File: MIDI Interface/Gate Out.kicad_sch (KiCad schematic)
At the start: 11 parts, among them J3 AudioJack2_SwitchT, U2 TL074

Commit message: Start MIDI interface board
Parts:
- C301: renamed from C25; footprint (none) -> 0_Capacitor_THT:C_Disc_D5.5mm_W2.5mm_P2.50mm
- C302: renamed from C26; footprint (none) -> 0_Capacitor_THT:C_Disc_D5.5mm_W2.5mm_P2.50mm
- D301: renamed from D8; footprint (none) -> LED_THT:LED_D5.0mm
- J301: renamed from J3; symbol Connector:AudioJack2_SwitchT -> Connector_Audio:AudioJack2_SwitchT
- R301: renamed from R7; footprint (none) -> Resistor_THT:R_Axial_DIN0207_L6.3mm_D2.5mm_P7.62mm_Horizontal
- R302: renamed from R8; footprint (none) -> Resistor_THT:R_Axial_DIN0207_L6.3mm_D2.5mm_P7.62mm_Horizontal
- R303: renamed from R9; footprint (none) -> Resistor_THT:R_Axial_DIN0207_L6.3mm_D2.5mm_P7.62mm_Horizontal
- R304: renamed from R10; footprint (none) -> Resistor_THT:R_Axial_DIN0207_L6.3mm_D2.5mm_P7.62mm_Horizontal
- R305: renamed from R11; footprint (none) -> Resistor_THT:R_Axial_DIN0207_L6.3mm_D2.5mm_P7.62mm_Horizontal
- R306: renamed from R12; footprint (none) -> Resistor_THT:R_Axial_DIN0207_L6.3mm_D2.5mm_P7.62mm_Horizontal
- U202: renamed from U2; footprint (none) -> Package_DIP:DIP-14_W7.62mm_Socket

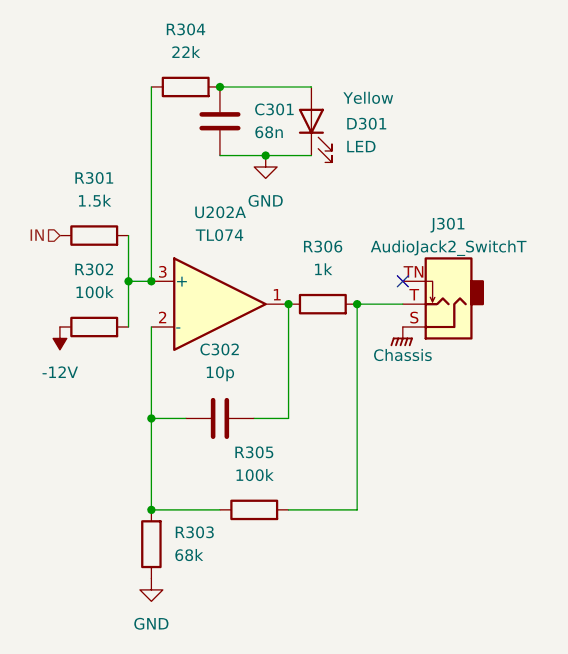
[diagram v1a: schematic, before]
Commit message: New MIDI controller, new envelope generator
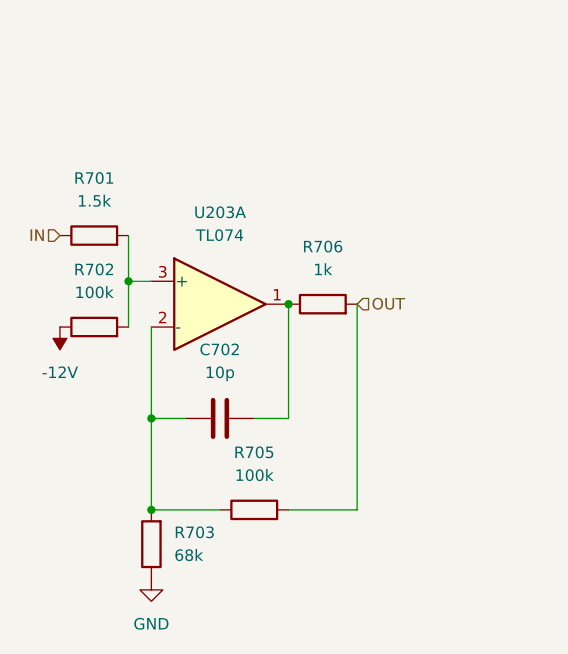
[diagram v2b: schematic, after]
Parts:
- removed C301: 68n, 0_Capacitor_THT:C_Disc_D5.5mm_W2.5mm_P2.50mm, symbol Device:C
- removed D301: LED, LED_THT:LED_D5.0mm, symbol Device:LED
- removed J301: AudioJack2_SwitchT, Connector_Audio:Jack_3.5mm_QingPu_WQP-PJ398SM_Vertical_CircularHoles, symbol Connector_Audio:AudioJack2_SwitchT
- removed R304: 22k, Resistor_THT:R_Axial_DIN0207_L6.3mm_D2.5mm_P7.62mm_Horizontal, symbol Device:R
- renumbered C302 to C702, R301 to R701, R302 to R702, R303 to R703, R305 to R705, R306 to R706, U202 to U203
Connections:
- net OUT: now reaches R705.2, R706.2
- no-connect marks 1 -> 0
